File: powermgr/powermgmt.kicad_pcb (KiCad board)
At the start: 2 copper layers, 83.8 x 40.1 mm, 58 parts, among them IC1 74HC4094_RevA_23Aug2012, IC2 AP24x1, IC3 AP24x1, IC4 AP24x1, IC5 AP24x1, IC6 AP24x1, IC7 AP24x1, IC8 AP24x1, IC9 AP24x1, J1 CONN_01X06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

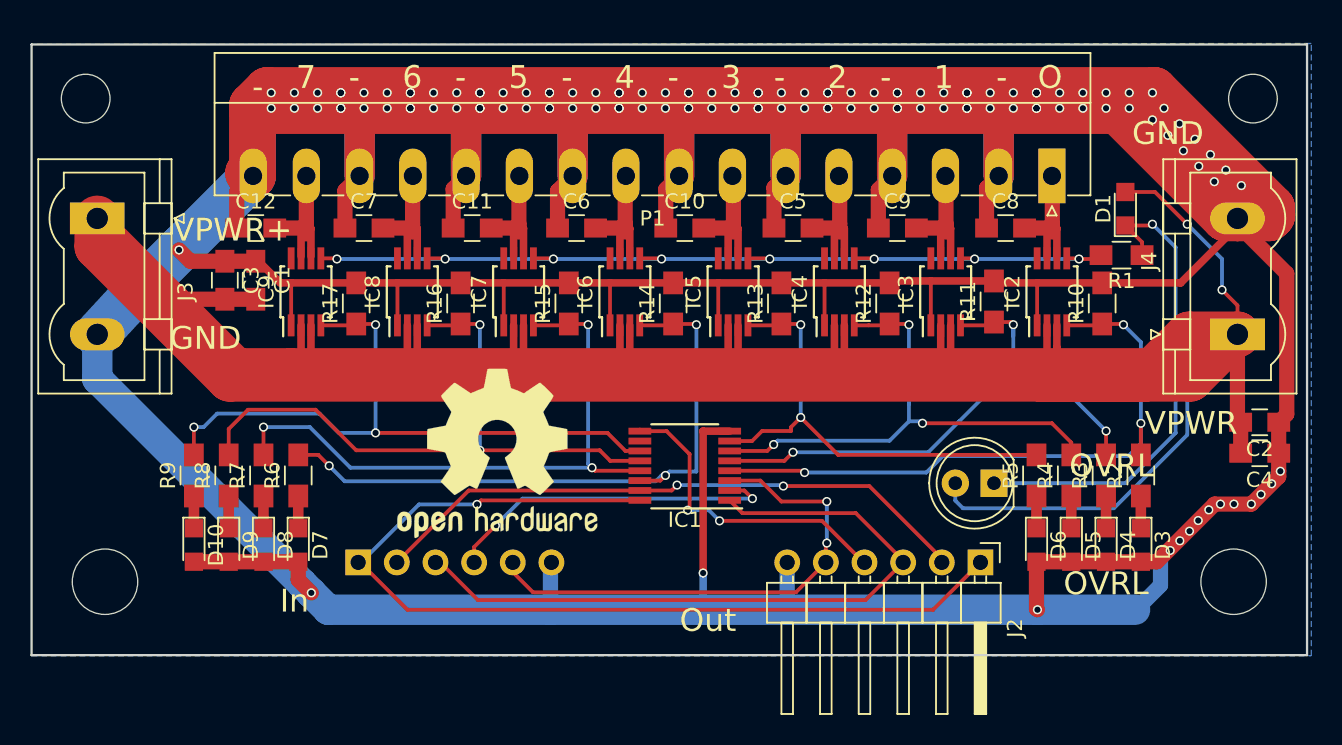
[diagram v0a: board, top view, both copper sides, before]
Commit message: so-8 version, I bought wrong part number..
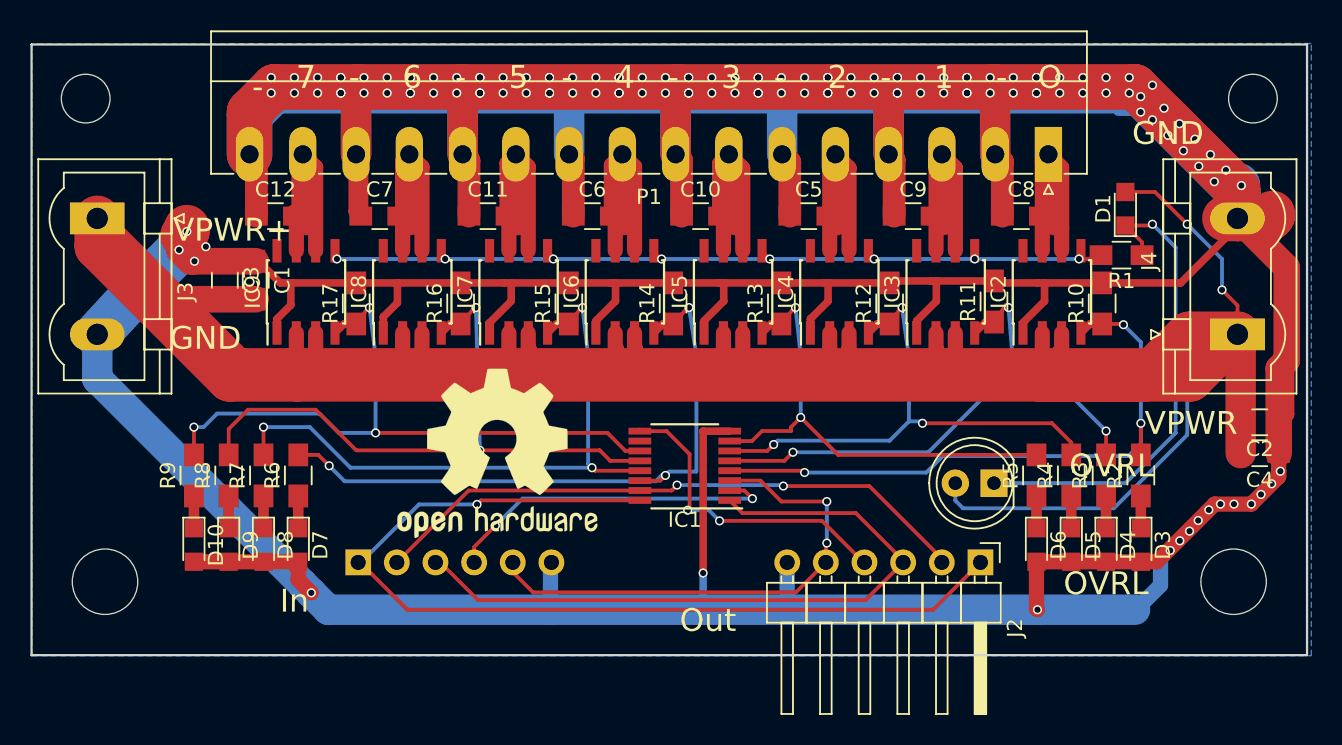
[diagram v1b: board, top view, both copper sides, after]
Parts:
- IC2, IC3, IC4, IC5, IC6, IC7, IC8, IC9: footprint Housings_SSOP:MSOP-8_3x3mm_Pitch0.65mm -> Housings_SOIC:SOIC-8_3.9x4.9mm_Pitch1.27mm
- moved C12 1.51 mm to (32.0, 26.0)
- moved P1 1.44 mm to (82.8, 21.9)
- moved C9 1.30 mm to (73.9, 26.0)
- moved C10 1.30 mm to (60.0, 26.0)
- moved C11 1.30 mm to (46.0, 26.0)
- moved C7 1.30 mm to (38.9, 26.0)
- moved C5 1.30 mm to (67.1, 26.0)
- moved C6 1.30 mm to (52.9, 26.0)
- moved C8 1.30 mm to (81.0, 26.0)
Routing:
- net GND: track 881.1 -> 714.8 mm, vias 125 -> 130
- net /Power out/out_pwr6: track 10.5 -> 23.0 mm
- net /Power out/out_pwr5: track 10.2 -> 22.4 mm
- net /Power out/out_pwr3: track 10.3 -> 22.5 mm
- net /Power out/out_pwr4: track 10.3 -> 22.4 mm
- net /Power out/out_pwr0: track 10.2 -> 18.7 mm
- net /Power out/out_pwr7: track 10.6 -> 18.9 mm
- net /Power out/out_pwr2: track 10.2 -> 18.1 mm
- net /Power out/out_pwr1: track 10.3 -> 18.1 mm
- net OVERLOAD: track 59.9 -> 54.6 mm
- net ctrl_out2: track 34.8 -> 36.8 mm
- net ctrl_out6: track 42.6 -> 43.4 mm
- net ctrl_out3: track 31.7 -> 32.5 mm
- net ctrl_out5: track 41.3 -> 42.1 mm
- net ctrl_out7: track 43.5 -> 44.2 mm
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
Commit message: fixups and text
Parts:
- added C13: 100n, Capacitors_SMD:C_0805_HandSoldering, F.Cu at (57.2, 46.8)
- IC1: value 74HC4094_RevA_23Aug2012 -> CD4094
- J1: value CONN_01X06 -> IN; footprint Pin_Headers:Pin_Header_Angled_1x06_Pitch2.54mm -> Pin_Headers:Pin_Header_Straight_1x06_Pitch2.54mm
- J2: value CONN_01X06 -> OUT; footprint Pin_Headers:Pin_Header_Angled_1x06_Pitch2.54mm -> Pin_Headers:Pin_Header_Straight_1x06_Pitch2.54mm
- P1: value CONN_01X16 -> PWR_OUT
- REF***: moved to B.Cu
- moved REF*** 45.6 mm to (92.1, 37.9), turned to 180 degrees
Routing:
- net GND: track 714.8 -> 745.3 mm, vias 130 -> 135
- net OVERLOAD: track 54.6 -> 59.8 mm
- net VCC: track 63.7 -> 65.8 mm
- net /Power out/out_pwr1: track 18.1 -> 19.0 mm
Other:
- board text added: "2A per out, 2.1-2.5 triggers current limit OVRL will lit if any outputs gets overloaded Outputs will have resistance if off (cap disch. func.) Controlling: CLK DATA in -> STROBE low -> ENABLE high ENA low will shut off all outputs"
- board text added: "3 2 1 0"
- board text added: "7 6 5 4"
- board text added: "CLK"
- board text added: "DATA IN"
- board text added: "DATA OUT"
- board text added: "ENA"
- board text added: "OVL"
- board text added: "STROBE"
- board text added: "VCC"
- board text added: "https://github.com/XANi/ee/tree/master/powermgr"

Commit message: fixes
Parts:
- removed the REF** at (96.3, 18.3)
- removed the REF** at (19.6, 18.3)
- added R18: 100k, Resistors_SMD:R_0805_HandSoldering, F.Cu at (77.5, 46.1)
- added REF**: MountingHole_4.3mm_M4, Mounting_Holes:MountingHole_4.3mm_M4, F.Cu at (20.9, 19.4)
- added REF**: MountingHole_4.3mm_M4, Mounting_Holes:MountingHole_4.3mm_M4, F.Cu at (95.0, 19.4)
- moved REF*** 2.57 mm to (92.1, 40.5)
- moved REF** 0.11 mm to (95.0, 50.1)
- moved REF** 0.11 mm to (20.9, 50.1)
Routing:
- net GND: track 745.3 -> 870.5 mm, vias 135 -> 137
- net VPWR: track 331.4 -> 353.4 mm
- net VCC: track 65.8 -> 77.4 mm
- net Net-(IC1-Pad15): track 40.2 -> 43.0 mm
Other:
- board text added: "D. OUT"
- board text removed: "DATA OUT"
